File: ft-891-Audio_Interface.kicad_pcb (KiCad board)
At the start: 2 copper layers, 57.5 x 30.5 mm, 13 parts, among them J1 Mic Cable, J2 Audio In, J3 Headset, J4 PTT, J5 Av Audio Jack, J6 Av Mic Jack

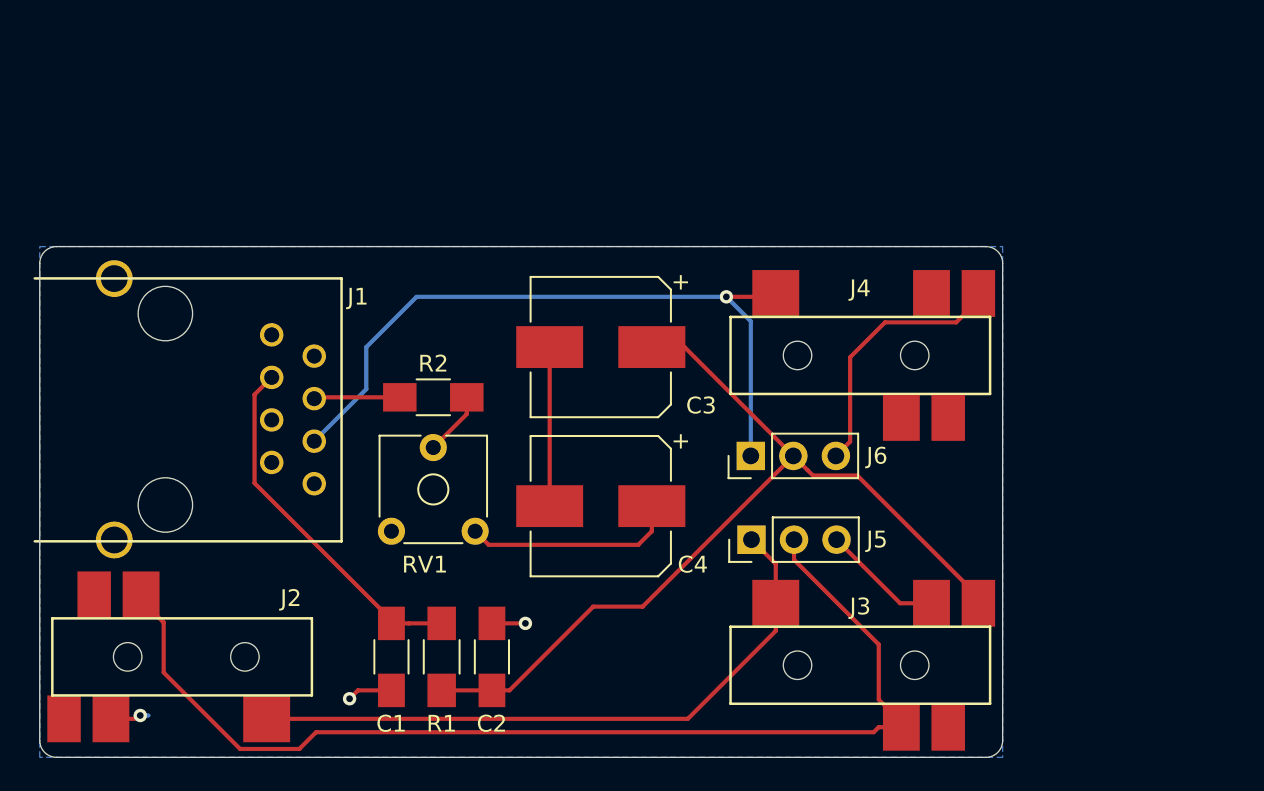
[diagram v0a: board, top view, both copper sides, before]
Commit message: Add expansion header and NPTH for mounting
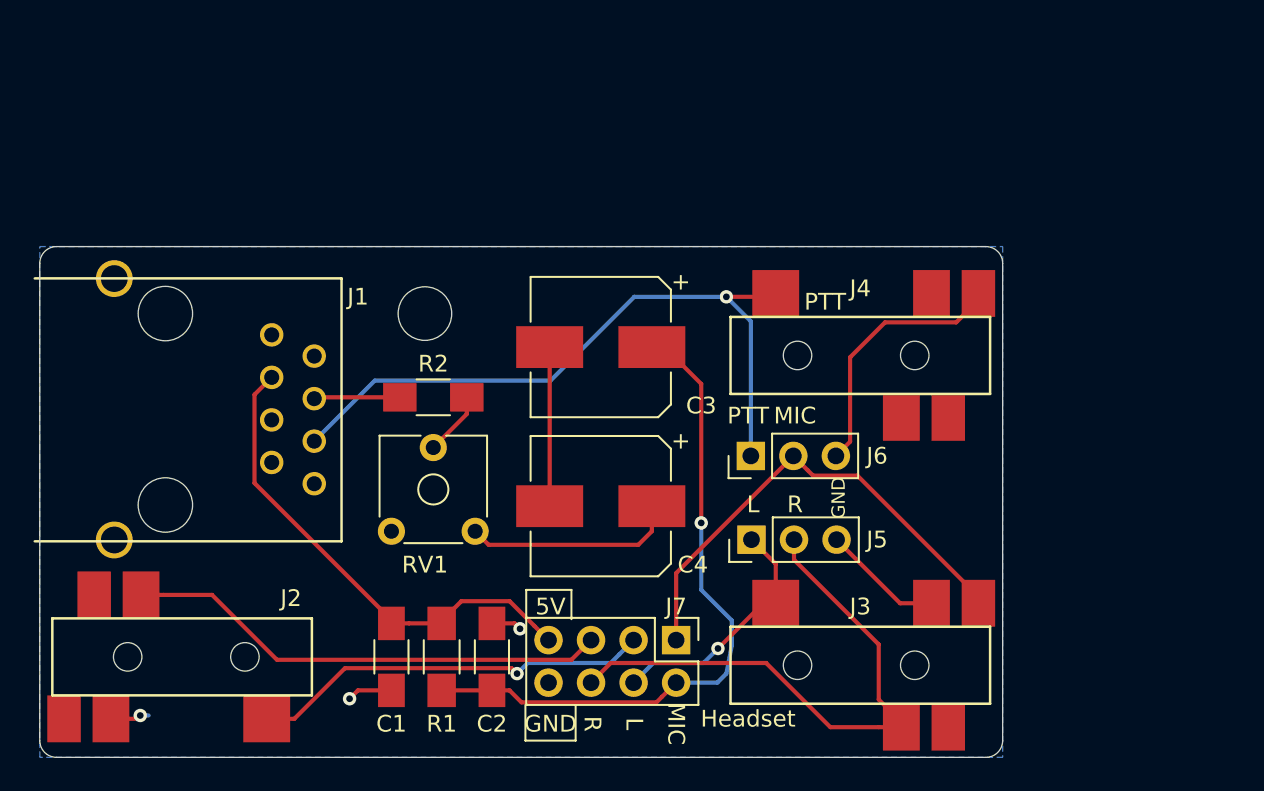
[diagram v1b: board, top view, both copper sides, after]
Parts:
- added J7: Audio Breakout, Pin_Headers:Pin_Header_Straight_2x04_Pitch2.54mm, F.Cu at (131.0, 120.0)
- added REF**: MountingHole_3.2mm_M3, Mounting_Holes:MountingHole_3.2mm_M3, F.Cu at (116.0, 100.5)
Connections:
- C2 pad 1: Av_Mic -> Mic_In
- C3 pad 1: Av_Mic -> Mic_In
- J3 pad 2: Audio_In_L -> Audio_Out_L
- J3 pad 3: Audio_In_R -> Audio_Out_R
- J5 pad 1: Audio_In_L -> Audio_Out_L
- J5 pad 2: Audio_In_R -> Audio_Out_R
- R1 pad 2: Av_Mic -> Mic_In
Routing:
- net Mic_In: track 0.00 -> 40.0 mm, vias 0 -> 1
- net Audio_In_R: track 65.5 -> 29.0 mm
- net Audio_Out_R: track 0.00 -> 34.5 mm
- net Av_Mic: track 52.9 -> 28.8 mm
- net Audio_Out_L: track 0.00 -> 14.9 mm, vias 0 -> 1
- net Audio_In_L: track 38.6 -> 24.1 mm, vias 0 -> 1
- net +5V: track 21.5 -> 29.5 mm
- net PTT: track 42.8 -> 41.3 mm
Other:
- board text added: "5V"
- board text added: "BVH - AB4EN FT-891 interface v1"
- board text added: "GND"
- board text added: "Headset"
- board text added: "L"
- board text added: "MIC"
- board text added: "Mic Bias voltage +3V Works with CTIA (LRGM) headsets"
- board text added: "PTT"
- board text added: "R"

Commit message: WIP
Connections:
- J1 pad 4: Audio_In_Gnd -> Mic
- J1 pad 5: Mic -> Audio_In_Gnd
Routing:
- net Mic: track 5.14 -> 8.21 mm
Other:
- board text added: "BVH - AB4EN FT-891 interface v2"
- board text removed: "BVH - AB4EN FT-891 interface v1"
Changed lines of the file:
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@@
     (thickness 1.6)
     (drawings 28)
-    (tracks 102)
+    (tracks 104)
     (zones 0)
     (modules 15)
@@
     (add_net "Net-(C3-Pad2)")
     (add_net "Net-(C4-Pad1)")
+    (add_net "Net-(J1-Pad1)")
+    (add_net "Net-(J1-Pad7)")
+    (add_net "Net-(J1-Pad8)")
+    (add_net "Net-(J2-Pad1)")
+    (add_net "Net-(J2-Pad6)")
+    (add_net "Net-(J3-Pad6)")
+    (add_net "Net-(J4-Pad3)")
+    (add_net "Net-(J4-Pad4)")
+    (add_net "Net-(J4-Pad6)")
     (add_net "Net-(R2-Pad1)")
     (add_net PTT)
@@
       (net 6 PTT))
     (pad 4 thru_hole circle (at 6.35 -6.35 270) (size 1.4 1.4) (drill 0.9) (layers *.Cu *.Mask)
-      (net 2 Audio_In_Gnd))
+      (net 7 Mic))
     (pad 5 thru_hole circle (at 5.08 -8.89 270) (size 1.4 1.4) (drill 0.9) (layers *.Cu *.Mask)
-      (net 7 Mic))
+      (net 2 Audio_In_Gnd))
     (pad 6 thru_hole circle (at 3.81 -6.35 270) (size 1.4 1.4) (drill 0.9) (layers *.Cu *.Mask)
       (net 1 +5V))
@@
     (effects (font (size 1 1) (thickness 0.15)) (justify mirror))
   )
-  (gr_text "BVH - AB4EN\nFT-891 interface v1" (at 126 104.5) (layer B.SilkS)
+  (gr_text "BVH - AB4EN\nFT-891 interface v2" (at 126 104.5) (layer B.SilkS)
     (effects (font (size 1.5 1.5) (thickness 0.3)) (justify mirror))
   )
@@
   (segment (start 131 116) (end 138 109) (width 0.25) (layer F.Cu) (net 3))
   (segment (start 131 120) (end 131 116) (width 0.25) (layer F.Cu) (net 3))
-  (segment (start 117 123) (end 120 123) (width 0.25) (layer F.Cu) (net 11))
   (segment (start 123.45 102.5) (end 123.45 112) (width 0.25) (layer F.Cu) (net 4))
   (segment (start 119.809999 114.309999) (end 119 113.5) (width 0.25) (layer F.Cu) (net 5))
@@
   (segment (start 128.5 99.5) (end 134 99.5) (width 0.25) (layer B.Cu) (net 6))
   (segment (start 123.5 104.5) (end 128.5 99.5) (width 0.25) (layer B.Cu) (net 6))
-  (segment (start 109.47 105.5) (end 109.39 105.58) (width 0.25) (layer F.Cu) (net 7))
-  (segment (start 114.5 105.5) (end 109.47 105.5) (width 0.25) (layer F.Cu) (net 7))
+  (segment (start 109.47 105.5) (end 109.39 105.58) (width 0.25) (layer F.Cu) (net 2))
+  (segment (start 114.35 105.5) (end 114.5 105.5) (width 0.25) (layer F.Cu) (net 7))
+  (segment (start 113 106.85) (end 114.35 105.5) (width 0.25) (layer F.Cu) (net 7))
+  (segment (start 106.85 106.85) (end 113 106.85) (width 0.25) (layer F.Cu) (net 7))
   (via (at 121.5 122) (size 0.8) (drill 0.4) (layers F.Cu B.Cu) (net 8))
   (segment (start 121.174999 121.674999) (end 121.5 122) (width 0.25) (layer F.Cu) (net 8))
@@
   (segment (start 124.744999 121.175001) (end 107.164003 121.175001) (width 0.25) (layer F.Cu) (net 9))
   (segment (start 125.92 120) (end 124.744999 121.175001) (width 0.25) (layer F.Cu) (net 9))
-  (segment (start 136.95 115.45) (end 135.5 114) (width 0.25) (layer F.Cu) (net 12))
-  (segment (start 136.95 117.8) (end 136.95 115.45) (width 0.25) (layer F.Cu) (net 12))
-  (segment (start 144.45 124.9) (end 144.45 125.2) (width 0.25) (layer F.Cu) (net 13))
-  (segment (start 143.1 123.55) (end 144.45 124.9) (width 0.25) (layer F.Cu) (net 13))
-  (segment (start 143.1 120.262081) (end 143.1 123.55) (width 0.25) (layer F.Cu) (net 13))
-  (segment (start 138.04 115.202081) (end 143.1 120.262081) (width 0.25) (layer F.Cu) (net 13))
-  (segment (start 138.04 114) (end 138.04 115.202081) (width 0.25) (layer F.Cu) (net 13))
   (segment (start 118.5 106.5) (end 118.5 105.5) (width 0.25) (layer F.Cu) (net 10))
   (segment (start 116.5 108.5) (end 118.5 106.5) (width 0.25) (layer F.Cu) (net 10))
+  (segment (start 117 123) (end 120 123) (width 0.25) (layer F.Cu) (net 11))
   (segment (start 129.824999 123.715001) (end 130.150001 123.389999) (width 0.25) (layer F.Cu) (net 11))
   (segment (start 121.765001 123.715001) (end 129.824999 123.715001) (width 0.25) (layer F.Cu) (net 11))
@@
   (segment (start 132.5 113) (end 132.5 117) (width 0.25) (layer B.Cu) (net 11))
   (segment (start 132.5 117) (end 134.324999 118.824999) (width 0.25) (layer B.Cu) (net 11))
+  (segment (start 136.95 115.45) (end 135.5 114) (width 0.25) (layer F.Cu) (net 12))
+  (segment (start 136.95 117.8) (end 136.95 115.45) (width 0.25) (layer F.Cu) (net 12))
   (via (at 133.5 120.5) (size 0.8) (drill 0.4) (layers F.Cu B.Cu) (net 12))
   (segment (start 132.635001 121.364999) (end 133.5 120.5) (width 0.25) (layer B.Cu) (net 12))
@@
   (segment (start 136.2 117.8) (end 136.95 117.8) (width 0.25) (layer F.Cu) (net 12))
   (segment (start 133.5 120.5) (end 136.2 117.8) (width 0.25) (layer F.Cu) (net 12))
+  (segment (start 144.45 124.9) (end 144.45 125.2) (width 0.25) (layer F.Cu) (net 13))
+  (segment (start 143.1 123.55) (end 144.45 124.9) (width 0.25) (layer F.Cu) (net 13))
+  (segment (start 143.1 120.262081) (end 143.1 123.55) (width 0.25) (layer F.Cu) (net 13))
+  (segment (start 138.04 115.202081) (end 143.1 120.262081) (width 0.25) (layer F.Cu) (net 13))
+  (segment (start 138.04 114) (end 138.04 115.202081) (width 0.25) (layer F.Cu) (net 13))
   (segment (start 136.375997 121.364999) (end 140.210998 125.2) (width 0.25) (layer F.Cu) (net 13))
   (segment (start 143.1 125.2) (end 144.45 125.2) (width 0.25) (layer F.Cu) (net 13))

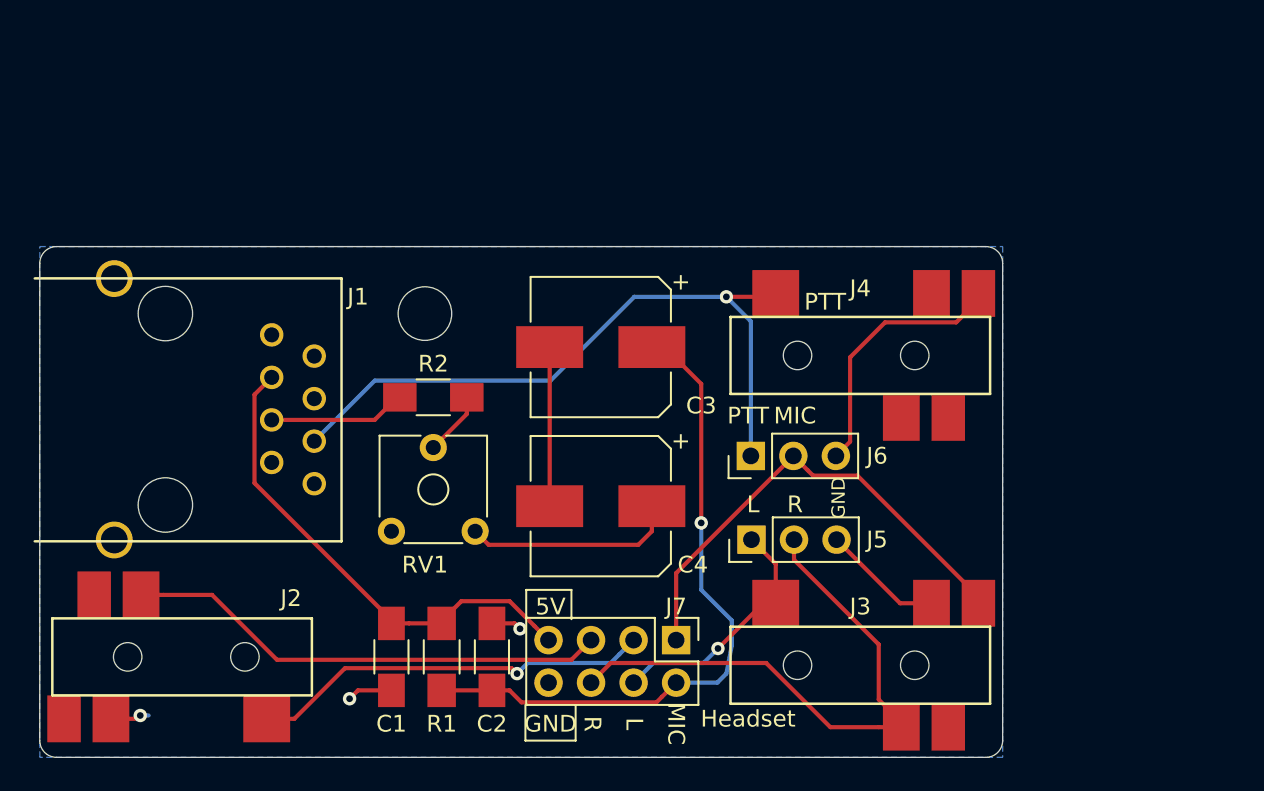
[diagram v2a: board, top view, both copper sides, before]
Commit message: FT-891 interface v2 - Fix earlier mistakes, larger board, mounting holes
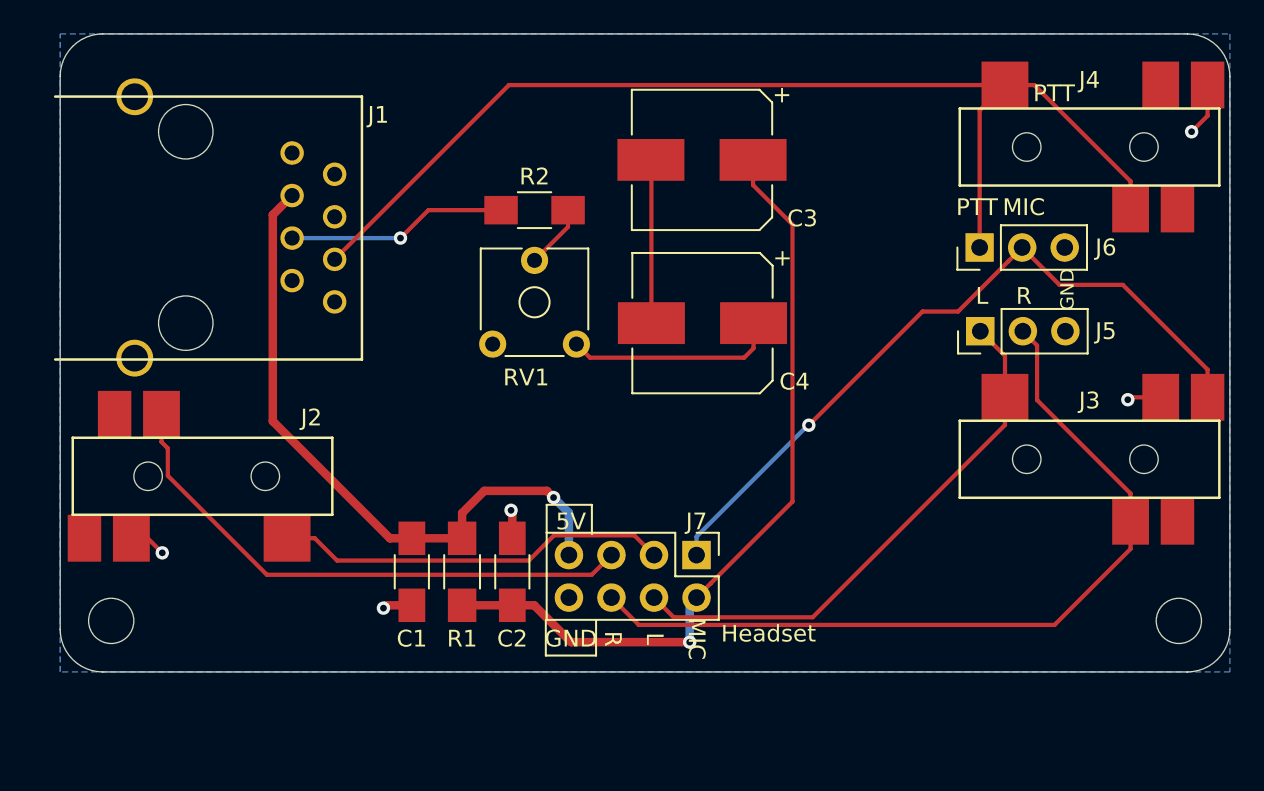
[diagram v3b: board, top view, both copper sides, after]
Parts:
- removed the REF** at (116.0, 100.5)
- added G***: LOGO, BVH_Logos:SkyIron_logo_Back, F.Cu at (110.7, 106.7)
- added REF**: MountingHole_2.7mm_M2.5, Mounting_Holes:MountingHole_2.7mm_M2.5, F.Cu at (97.3, 118.9)
- added REF**: MountingHole_2.7mm_M2.5, Mounting_Holes:MountingHole_2.7mm_M2.5, F.Cu at (161.0, 118.9)
- moved J4 18.5 mm to (155.7, 90.6)
- moved J5 18.5 mm to (149.2, 101.6)
- moved J6 18.5 mm to (149.1, 96.6)
- moved J3 18.4 mm to (155.7, 109.2)
- moved C3 12.7 mm to (132.5, 91.3)
- moved R2 12.7 mm to (122.5, 94.3)
- moved RV1 12.7 mm to (125.0, 102.3)
- moved C4 12.5 mm to (132.6, 101.1)
- moved J1 10.9 mm to (101.7, 89.6)
- moved J2 10.9 mm to (102.7, 110.2)
- moved C1 5.22 mm to (115.2, 115.9)
- moved C2 5.22 mm to (121.2, 115.9)
- moved J7 5.22 mm to (132.2, 114.9)
- moved R1 5.22 mm to (118.2, 115.9)
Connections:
- J4 pad 3: (no net) -> PTT
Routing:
- net PTT: track 41.3 -> 66.5 mm, vias 1 -> 0
- net Audio_In_Gnd: track 29.9 -> 11.3 mm, vias 3 -> 5
- net Audio_Out_L: track 14.9 -> 32.4 mm, vias 1 -> 0
- net Audio_Out_R: track 34.5 -> 49.2 mm
- net Av_Mic: track 28.8 -> 43.4 mm, vias 0 -> 1
- net +5V: track 29.5 -> 39.7 mm, vias 0 -> 1
- net Mic_In: track 40.0 -> 47.6 mm
- net Mic: track 8.21 -> 13.2 mm, vias 0 -> 1
- net Audio_In_R: track 29.0 -> 33.3 mm
- net Audio_In_L: track 24.1 -> 23.6 mm, vias 1 -> 0
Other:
- board size 57.5 x 30.5 mm -> 69.9 x 38.1 mm
- board text added: "BVH - AB4EN FT-891 interface 2020-05 v2"
- board text removed: "BVH - AB4EN FT-891 interface v2"
